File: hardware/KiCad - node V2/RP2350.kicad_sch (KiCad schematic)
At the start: 87 parts, among them J3 USB_C_Receptacle_USB2.0_14P, SW1 BOOTSEL, U1 RP2350A, U2 THVD1450D, U3 ADXL355BEZ, U4 TPS2121RUXR, U5 USBLC6-2SC6, U6 TLV75733PDBV, U7 W25Q128JVS, U8 TPS7A20xxxDBV

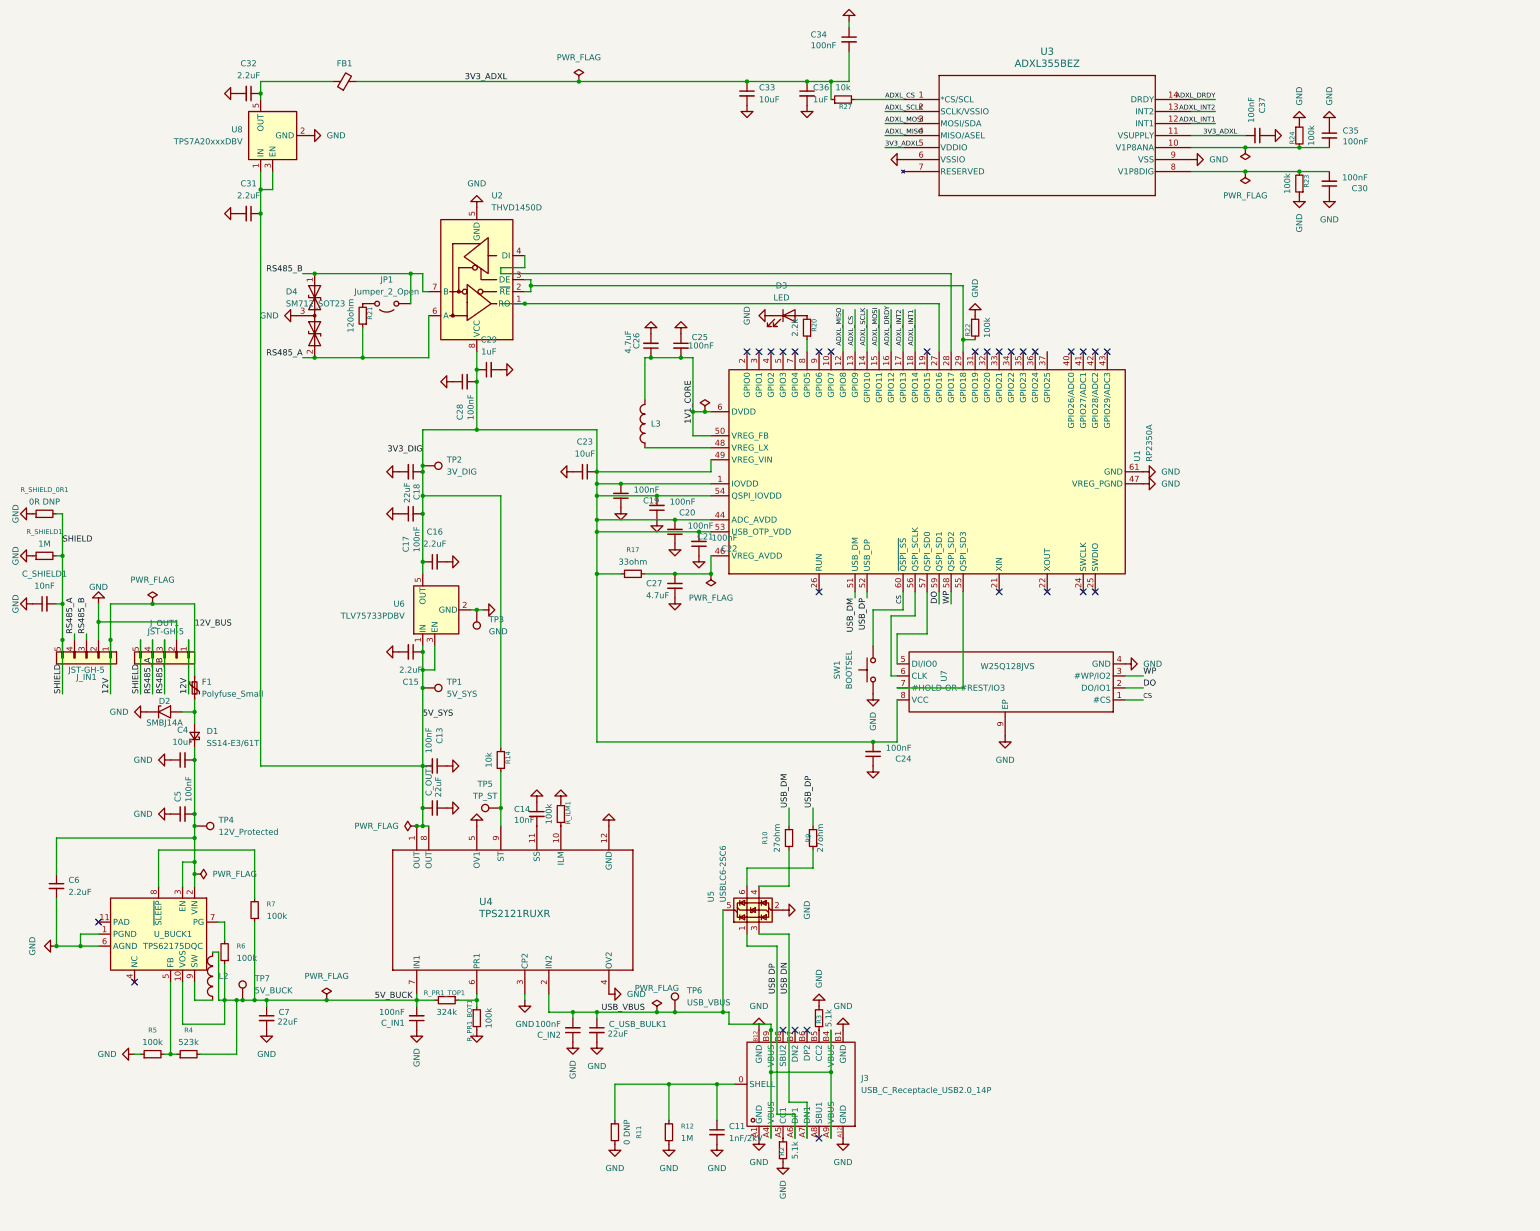
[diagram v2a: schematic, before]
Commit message: hardware: added footprints, part numbers, layout update
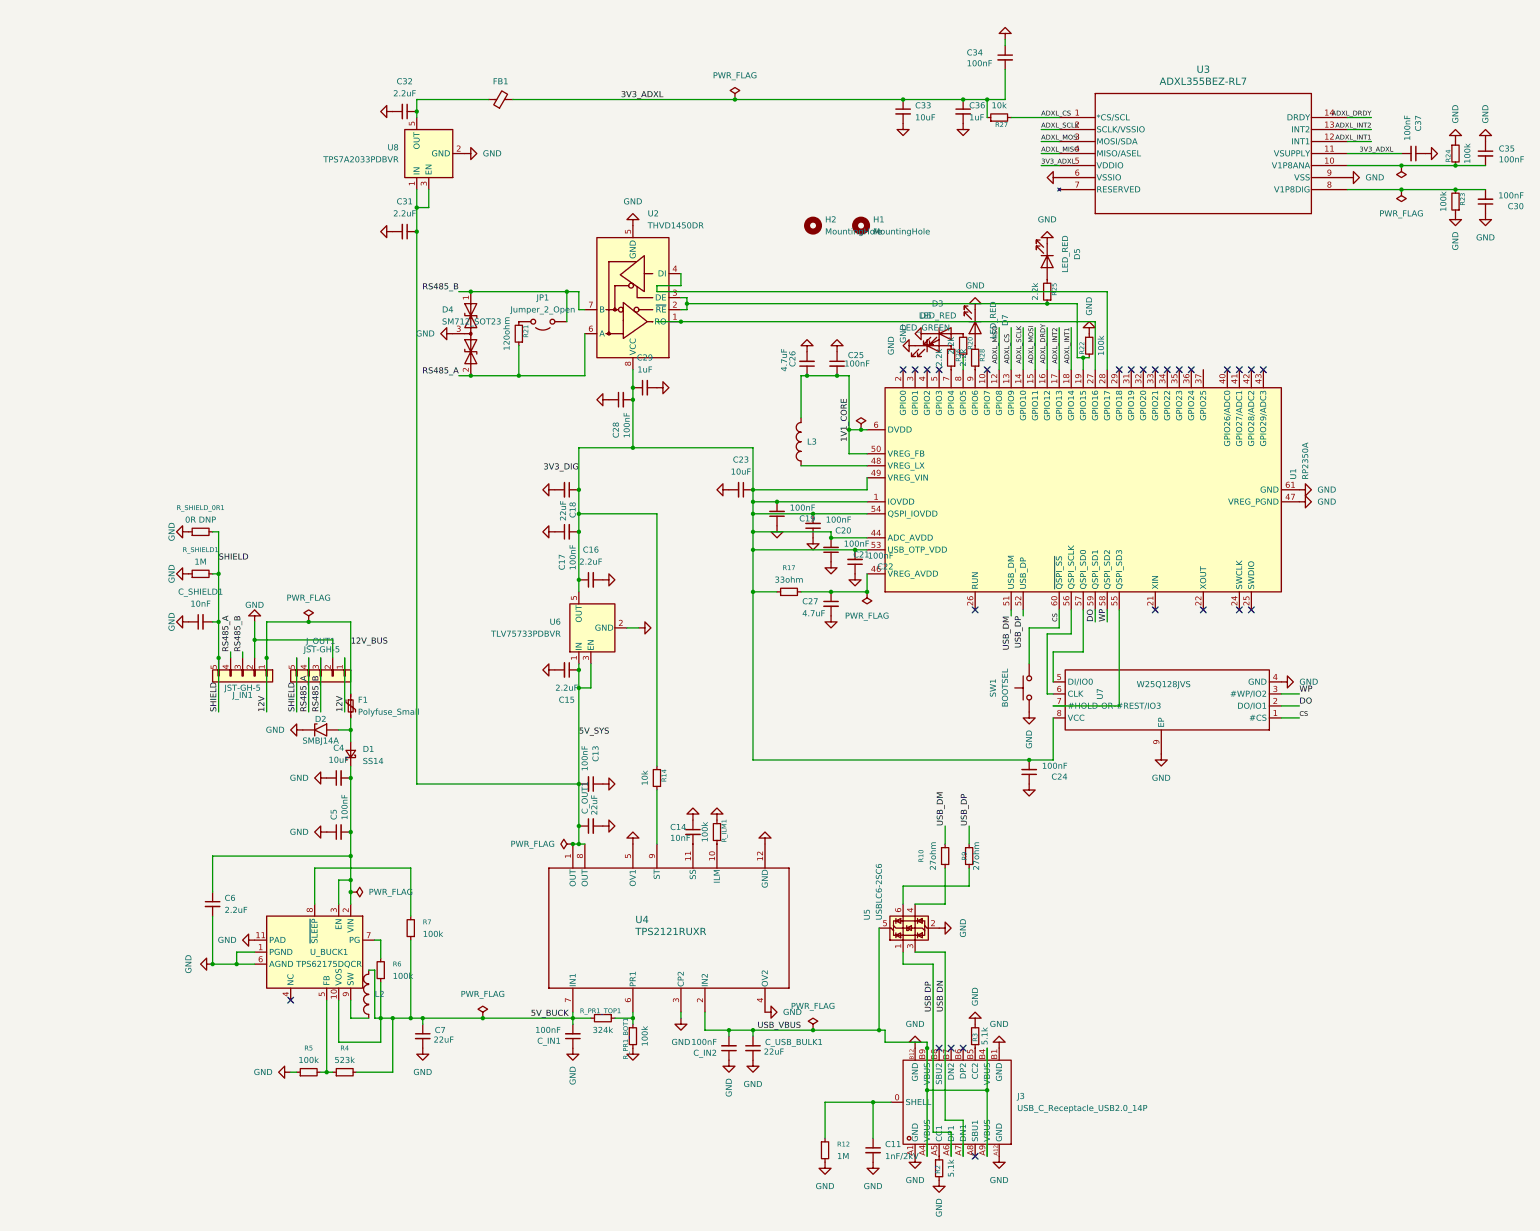
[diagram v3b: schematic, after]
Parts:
- removed R11: 0 DNP, Resistor_SMD:R_0805_2012Metric, symbol Device:R_Small
- removed TP1: 5V_SYS, Connector_Pin:Pin_D0.7mm_L6.5mm_W1.8mm_FlatFork, symbol Connector:TestPoint
- removed TP2: 3V_DIG, symbol Connector:TestPoint
- removed TP3: GND, symbol Connector:TestPoint
- removed TP4: 12V_Protected, Connector_Pin:Pin_D0.7mm_L6.5mm_W1.8mm_FlatFork, symbol Connector:TestPoint
- removed TP5: TP_ST, symbol Connector:TestPoint
- removed TP6: USB_VBUS, symbol Connector:TestPoint
- removed TP7: 5V_BUCK, symbol Connector:TestPoint
- added D5, D7: LED_RED, LED_SMD:LED_0603_1608Metric, symbol Device:LED
- added D6: LED_GREEN, LED_SMD:LED_0805_2012Metric, symbol Device:LED
- added H1, H2: MountingHole, MountingHole:MountingHole_2.5mm, symbol Mechanical:MountingHole
- added R25, R26, R28: 2.2k, Resistor_SMD:R_0402_1005Metric, symbol Device:R_Small
- D1: value SS14-E3/61T -> SS14; JLCPC# (none) -> SS14; Manufacturer Part (none) -> SS14
- D2: JLCPC# (none) -> C29937; Manufacturer Part (none) -> SMBJ14A
- D3: value LED -> LED_RED; JLCPC# (none) -> 0603; Manufacturer Part (none) -> KT-0603R
- D4: JLCPC# (none) -> C12067; Manufacturer Part (none) -> SM712.TCT
- F1: JLCPC# (none) -> C142805; Manufacturer Part (none) -> 1812L150/24MR
- FB1: JLCPC# (none) -> C21519; Manufacturer Part (none) -> MPZ2012S601AT000
- J3: footprint GT-USB-7051A:USB-C-SMD_GT-USB-7051A -> footprints:USB-C-SMD_GT-USB-7051A; JLCPC# (none) -> C2843970
- JP1: footprint (none) -> Jumper:SolderJumper-2_P1.3mm_Open_Pad1.0x1.5mm
- J_IN1, J_OUT1: JLCPC# (none) -> C189891; Manufacturer Part (none) -> BM05B-GHS-TBT(LF)(SN)(N)
- L2: JLCPC# (none) -> C177242
- L3: JLCPC# (none) -> C42411119
- R20: footprint Resistor_SMD:R_0603_1608Metric -> Resistor_SMD:R_0402_1005Metric
- SW1: JLCPC# (none) -> C139797; Manufacturer Part (none) -> SKRPACE010
- U1: JLCPC# (none) -> C42411118
- U2: value THVD1450D -> THVD1450DR; footprint Package_SO:SOIC-8_3.9x4.9mm_P1.27mm -> footprints:THVD1450DR-SOIC-8_L4.9-W3.9-P1.27-LS6.0-BL; JLCPC# (none) -> C2671361
- U3: value ADXL355BEZ -> ADXL355BEZ-RL7; footprint my_footprints:E-14-1_ADI-M -> footprints:ADXL355BEZ-RL7; JLCPC# (none) -> C515892
- U4: footprint my_footprints:RUX0012A -> footprints:TPS2121RUXR-VQFN-HR-12_L2.5-W2.0-P0.50-BL; JLCPC# (none) -> C485916
- U5: JLCPC# (none) -> C7519
- U6: value TLV75733PDBV -> TLV75733PDBVR; footprint Package_TO_SOT_SMD:SOT-23-5 -> footprints:TLV75733PDBVR-SOT-23-5_L2.9-W1.6-P0.95-LS2.8-BL; JLCPC# (none) -> C485517; Manufacturer Part (none) -> TLV75733PDBVR
- U7: JLCPC# (none) -> C190862
- U8: value TPS7A20xxxDBV -> TPS7A2033PDBVR; footprint Package_TO_SOT_SMD:SOT-23-5 -> footprints:TPS7A2033PDBVR; JLCPC# (none) -> C2862740; Manufacturer Part (none) -> TPS7A2033PDBVR
- U_BUCK1: value TPS62175DQC -> TPS62175DQCR; footprint Package_SON:WSON-10-1EP_2x3mm_P0.5mm_EP0.84x2.4mm_ThermalVias -> footprints:TPS62175DQCR_WSON-10_L3.0-W2.0-P0.50-BL-EP; JLCPC# (none) -> C32097; Manufacturer Part (none) -> TPS62175DQCR
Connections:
- net GND: now also U_BUCK1.11 (PAD), D5.1 (K), D6.1 (K), D7.1 (K)
- net at R22.2, U2.2 (~{RE}), U2.3 (DE): now also U1.19 (GPIO15), R25.1; no longer U1.29 (GPIO18)
- net at U1.7 (GPIO4): now also R26.1
- net at U1.9 (GPIO6): now also R28.1
- new net: D6.2 (A), R26.2
- new net: D7.2 (A), R28.2
- new net: D5.2 (A), R25.2
- no-connect marks 29 -> 26
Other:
- moved on the sheet: C11, C13, C14, C15, C16, C17, C18, C19, C20, C21, C22, C23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
